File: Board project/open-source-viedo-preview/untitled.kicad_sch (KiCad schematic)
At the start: 1 part

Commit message: Imporoved electrical schematic
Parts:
- gave numbers to parts that had none: 1
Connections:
- net +12v renamed +12V
- net +3.3v renamed +3V3
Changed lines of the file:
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@@
 (kicad_sch (version 20201015) (generator eeschema)
+  (page 1 6)
   (paper "A4")
   (junction (at 130.81 92.71) (diameter 1.016) (color 0 0 0 0))
@@
   (junction (at 166.37 95.25) (diameter 1.016) (color 0 0 0 0))
   (no_connect (at 133.35 85.09))
+  (no_connect (at 162.56 74.93))
   (no_connect (at 133.35 87.63))
+  (no_connect (at 133.35 115.57))
+  (no_connect (at 162.56 90.17))
   (no_connect (at 133.35 100.33))
-  (no_connect (at 133.35 115.57))
-  (no_connect (at 162.56 74.93))
-  (no_connect (at 162.56 90.17))
-  (wire (pts (xy 118.745 74.93) (xy 133.35 74.93))
-    (stroke (width 0) (type solid) (color 0 0 0 0))
-  )
   (wire (pts (xy 119.38 92.71) (xy 130.81 92.71))
+    (stroke (width 0) (type solid) (color 0 0 0 0))
+  )
+  (wire (pts (xy 125.73 73.66) (xy 125.73 74.93))
+    (stroke (width 0) (type solid) (color 0 0 0 0))
+  )
+  (wire (pts (xy 125.73 74.93) (xy 133.35 74.93))
     (stroke (width 0) (type solid) (color 0 0 0 0))
   )
@@
     (effects (font (size 1.27 1.27)) (justify right bottom))
   )
-  (label "+12v" (at 121.92 74.93 0)
-    (effects (font (size 1.27 1.27)) (justify left bottom))
-  )
-  (label "+3.3v" (at 121.92 92.71 0)
-    (effects (font (size 1.27 1.27)) (justify left bottom))
-  )
-  (label "+12v" (at 167.64 77.47 0)
-    (effects (font (size 1.27 1.27)) (justify left bottom))
-  )
-  (label "+3.3v" (at 167.64 85.09 0)
-    (effects (font (size 1.27 1.27)) (justify left bottom))
-  )
   (hierarchical_label "PCIE_CLK_nREQ" (shape output) (at 118.11 102.87 180)
     (effects (font (size 1.27 1.27)) (justify right))
@@
     (effects (font (size 1.27 1.27)) (justify right))
   )
-  (hierarchical_label "+12v" (shape input) (at 118.745 74.93 180)
-    (effects (font (size 1.27 1.27)) (justify right))
-  )
   (hierarchical_label "PCIE_nRST" (shape input) (at 176.53 100.33 0)
     (effects (font (size 1.27 1.27)) (justify left))
@@
     (effects (font (size 1.27 1.27)) (justify left))
   )
-  (symbol (lib_id "power:GND") (at 132.08 121.92 0)
-    (in_bom yes) (on_board yes)
-    (property "Reference" "#PWR?" (id 0) (at 132.08 128.27 0)
+  (symbol (lib_id "power:+3V3") (at 119.38 92.71 0) (unit 1)
+    (in_bom yes) (on_board yes)
+    (property "Reference" "#PWR057" (id 0) (at 119.38 96.52 0)
+      (effects (font (size 1.27 1.27)) hide)
+    )
+    (property "Value" "+3V3" (id 1) (at 119.7483 88.3856 0))
+    (property "Footprint" "" (id 2) (at 119.38 92.71 0)
+      (effects (font (size 1.27 1.27)) hide)
+    )
+    (property "Datasheet" "" (id 3) (at 119.38 92.71 0)
+      (effects (font (size 1.27 1.27)) hide)
+    )
+  )
+  (symbol (lib_id "power:+12V") (at 125.73 73.66 0) (unit 1)
+    (in_bom yes) (on_board yes)
+    (property "Reference" "#PWR042" (id 0) (at 125.73 77.47 0)
+      (effects (font (size 1.27 1.27)) hide)
+    )
+    (property "Value" "+12V" (id 1) (at 126.0983 69.3356 0))
+    (property "Footprint" "" (id 2) (at 125.73 73.66 0)
+      (effects (font (size 1.27 1.27)) hide)
+    )
+    (property "Datasheet" "" (id 3) (at 125.73 73.66 0)
+      (effects (font (size 1.27 1.27)) hide)
+    )
+  )
+  (symbol (lib_id "power:+12V") (at 172.72 77.47 0) (unit 1)
+    (in_bom yes) (on_board yes)
+    (property "Reference" "#PWR045" (id 0) (at 172.72 81.28 0)
+      (effects (font (size 1.27 1.27)) hide)
+    )
+    (property "Value" "+12V" (id 1) (at 173.0883 73.1456 0))
+    (property "Footprint" "" (id 2) (at 172.72 77.47 0)
+      (effects (font (size 1.27 1.27)) hide)
+    )
+    (property "Datasheet" "" (id 3) (at 172.72 77.47 0)
+      (effects (font (size 1.27 1.27)) hide)
+    )
+  )
+  (symbol (lib_id "power:+3V3") (at 172.72 85.09 0) (unit 1)
+    (in_bom yes) (on_board yes)
+    (property "Reference" "#PWR058" (id 0) (at 172.72 88.9 0)
+      (effects (font (size 1.27 1.27)) hide)
+    )
+    (property "Value" "+3V3" (id 1) (at 173.0883 80.7656 0))
+    (property "Footprint" "" (id 2) (at 172.72 85.09 0)
+      (effects (font (size 1.27 1.27)) hide)
+    )
+    (property "Datasheet" "" (id 3) (at 172.72 85.09 0)
+      (effects (font (size 1.27 1.27)) hide)
+    )
+  )
+  (symbol (lib_id "power:GND") (at 132.08 121.92 0) (unit 1)
+    (in_bom yes) (on_board yes)
+    (property "Reference" "#PWR043" (id 0) (at 132.08 128.27 0)
       (effects (font (size 1.27 1.27)) hide)
     )
@@
     )
   )
-  (symbol (lib_id "power:GND") (at 163.83 121.92 0)
-    (in_bom yes) (on_board yes)
-    (property "Reference" "#PWR?" (id 0) (at 163.83 128.27 0)
+  (symbol (lib_id "power:GND") (at 163.83 121.92 0) (unit 1)
+    (in_bom yes) (on_board yes)
+    (property "Reference" "#PWR044" (id 0) (at 163.83 128.27 0)
       (effects (font (size 1.27 1.27)) hide)
     )
@@
     )
   )
-  (symbol (lib_id "CM4IO:PCIe-x1") (at 152.4 107.95 0)
-    (in_bom yes) (on_board yes)
-    (property "Reference" "J?" (id 0) (at 156.21 71.12 0))
+  (symbol (lib_id "CM4IO:PCIe-x1") (at 152.4 107.95 0) (unit 1)
+    (in_bom yes) (on_board yes)
+    (property "Reference" "J13" (id 0) (at 156.21 71.12 0))
     (property "Value" "10018783-11200TLF" (id 1) (at 147.955 70.5104 0))
     (property "Footprint" "CM4IO:PCIex1-36" (id 2) (at 152.4 107.95 0)

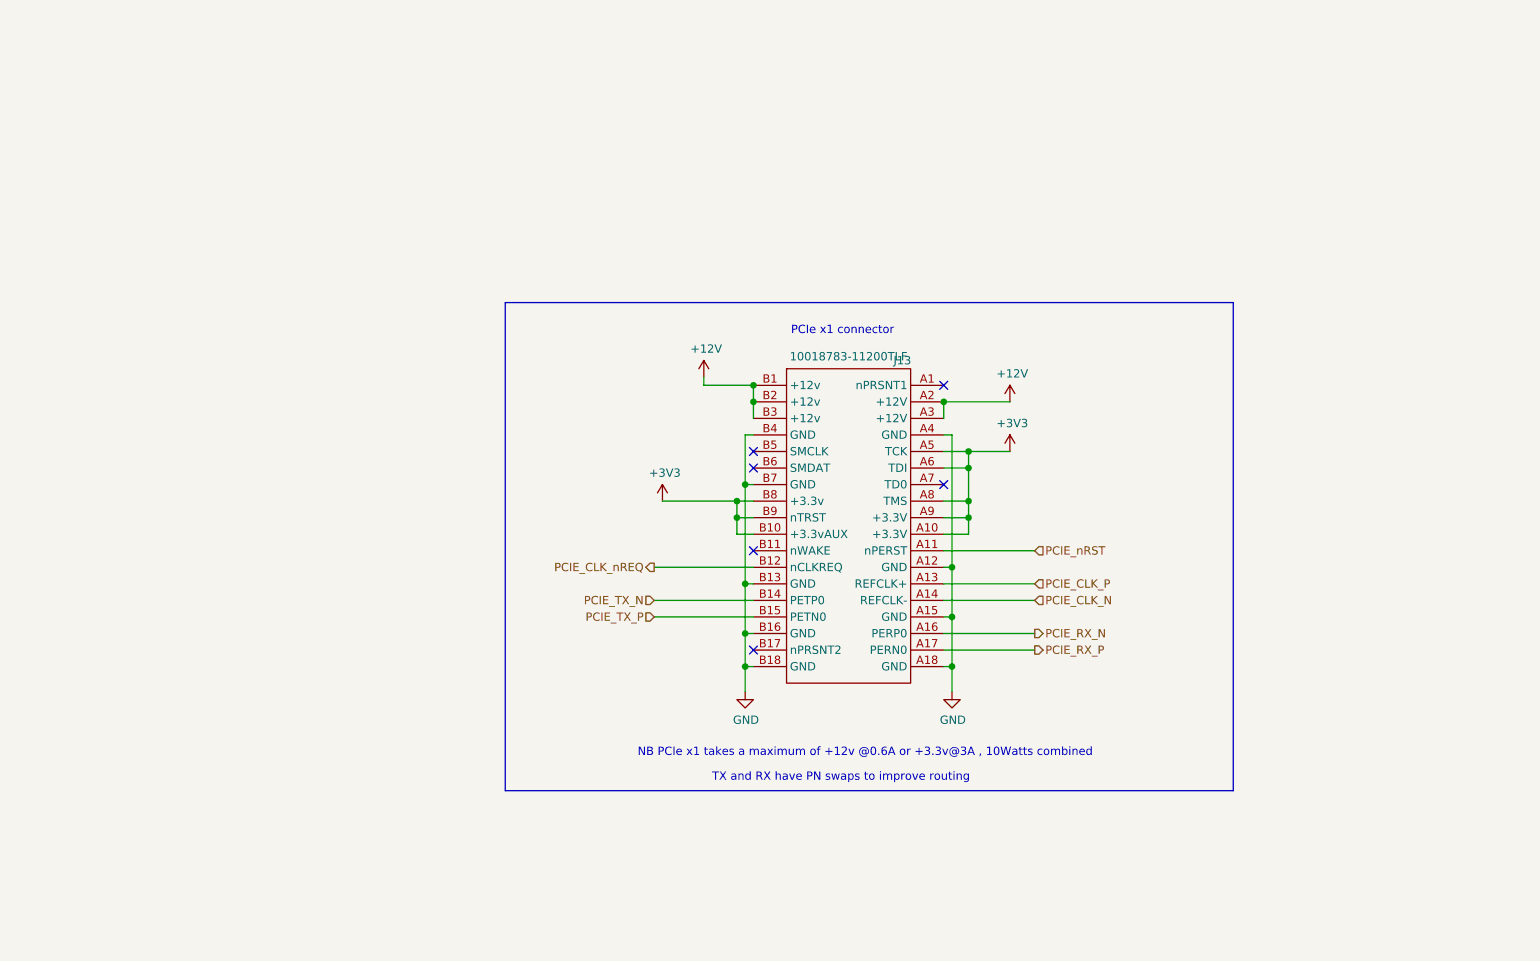
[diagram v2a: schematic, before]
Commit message: added 3.3v power supply for PCIe
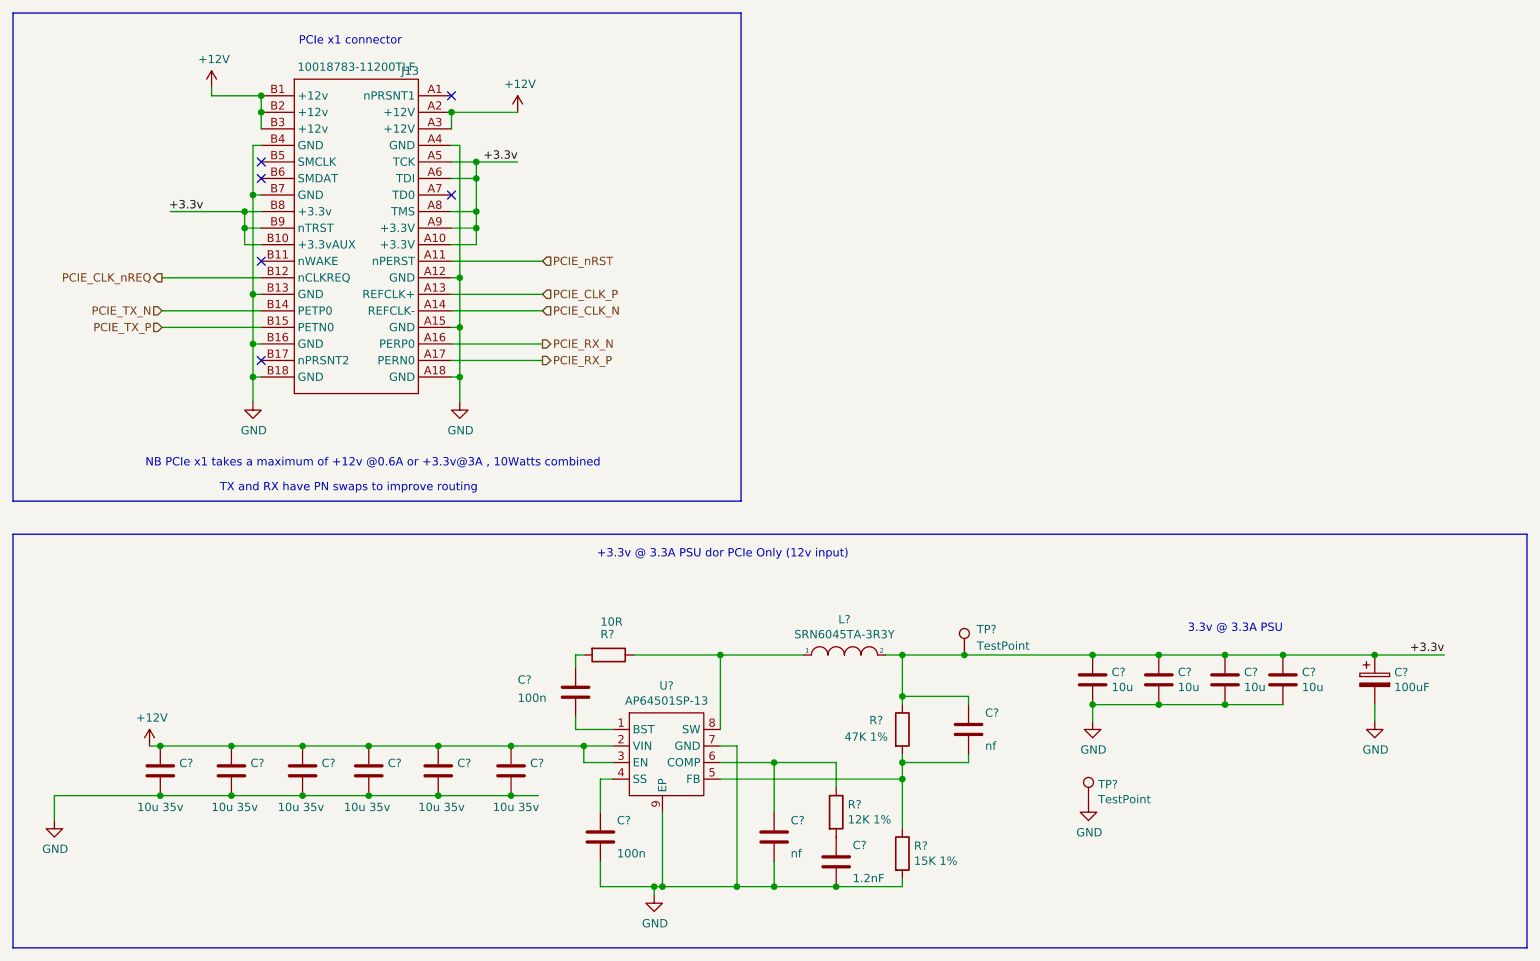
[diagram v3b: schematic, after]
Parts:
- added C? (x4): 10u, Capacitor_SMD:C_0805_2012Metric, symbol Device:C
- added C? (x6): 10u 35v, Capacitor_SMD:C_0805_2012Metric, symbol Device:C
- added C? (x2): 100n, Capacitor_SMD:C_0402_1005Metric, symbol Device:C
- added C?: 100uF, Capacitor_Tantalum_SMD:CP_EIA-7343-31_Kemet-D, symbol Device:CP
- added C? (x2): nf, Capacitor_SMD:C_0402_1005Metric, symbol Device:C
- added C?: 1.2nF, Capacitor_SMD:C_0402_1005Metric, symbol Device:C
- added L?: SRN6045TA-3R3Y, Inductor_SMD:L_Bourns_SRN6045TA, symbol pspice:INDUCTOR
- added R?: 12K 1%, Resistor_SMD:R_0402_1005Metric, symbol Device:R
- added R?: 10R, Resistor_SMD:R_0402_1005Metric, symbol Device:R
- added R?: 47K 1%, Resistor_SMD:R_0402_1005Metric, symbol Device:R
- added R?: 15K 1%, Resistor_SMD:R_0402_1005Metric, symbol Device:R
- added TP? (x2): TestPoint, TestPoint:TestPoint_Pad_2.0x2.0mm, symbol Connector:TestPoint
- added U?: AP64501SP-13, Package_SO:SOIC-8-1EP_3.9x4.9mm_P1.27mm_EP2.95x4.9mm_Mask2.71x3.4mm_ThermalVias, symbol CM4IO:AP64351
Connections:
- net +12V: now also C?.1, C?.1, C?.1, C?.1, C?.1, C?.1, U?.2 (VIN), U?.3 (EN)
- net GND: now also C?.2, C?.2, C?.2, C?.2, C?.2, C?.2, C?.2, C?.2, C?.2, C?.2, C?.2, C?.2, C?.2, C?.2, R?.2, TP?.1, U?.7 (GND), U?.9 (EP)
- net +3V3 renamed +3.3v
- new net: C?.1, C?.1, C?.1, C?.1, C?.1, C?.1, L?.2, R?.1, TP?.1
- new net: C?.1, R?.1, U?.6 (COMP)
- new net: C?.1, R?.2 (x2)
- new net: C?.1, U?.4 (SS)
- new net: C?.2, R?.1, R?.2, U?.5 (FB)
- new net: L?.1, R?.1, U?.8 (SW)
- new net: C?.2, U?.1 (BST)
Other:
- note added: "+3.3v @ 3.3A PSU dor PCIe Only (12v input)"
- note added: "3.3v @ 3.3A PSU"
- moved on the sheet: J13

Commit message: ERC error repaired
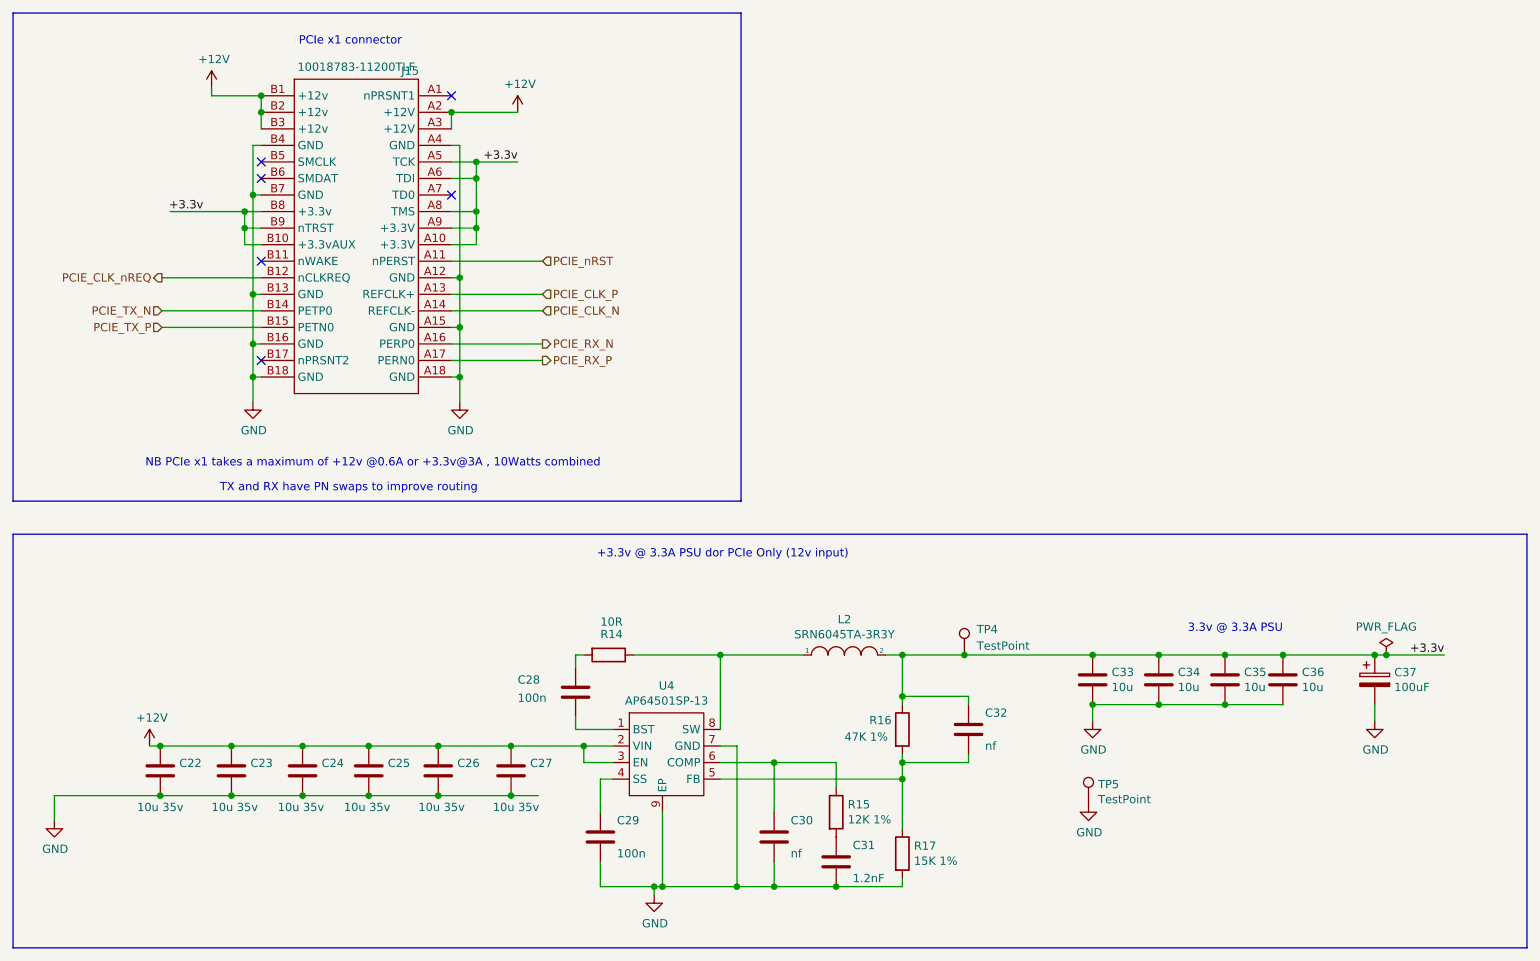
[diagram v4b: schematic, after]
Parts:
- gave numbers to parts that had none: 24
- renumbered J13 to J15
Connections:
- net +3.3v: now also C32.1, C33.1, C34.1, C35.1, C36.1, C37.1, L2.2, R16.1, TP4.1
